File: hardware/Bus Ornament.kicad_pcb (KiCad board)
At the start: 4 copper layers, 110 x 57.8 mm, 35 parts, among them J1 Conn_02x03_Odd_Even, SW1 SW_SPST, SW2 SW_Push, U1 ATtiny85-20PU, U2 TPS62203DBV

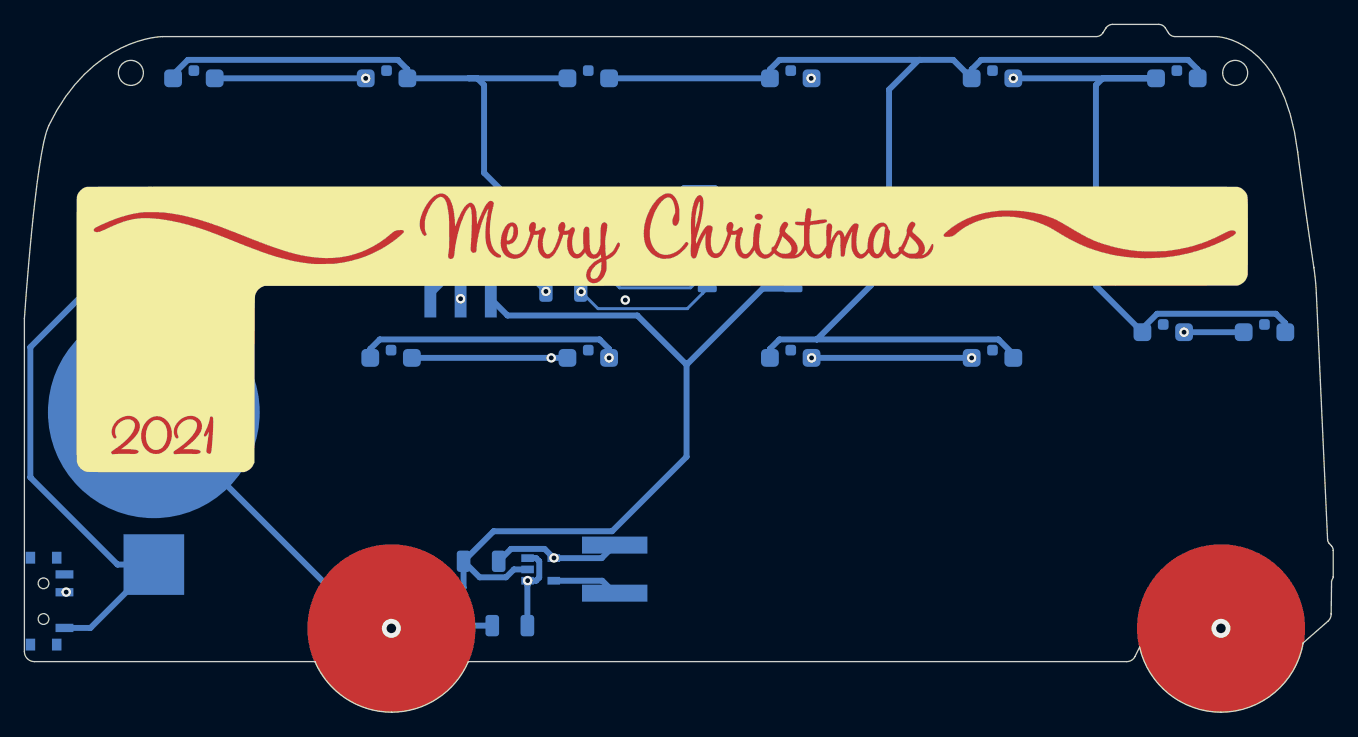
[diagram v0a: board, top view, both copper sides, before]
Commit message: Crated front fill, ordered new boards
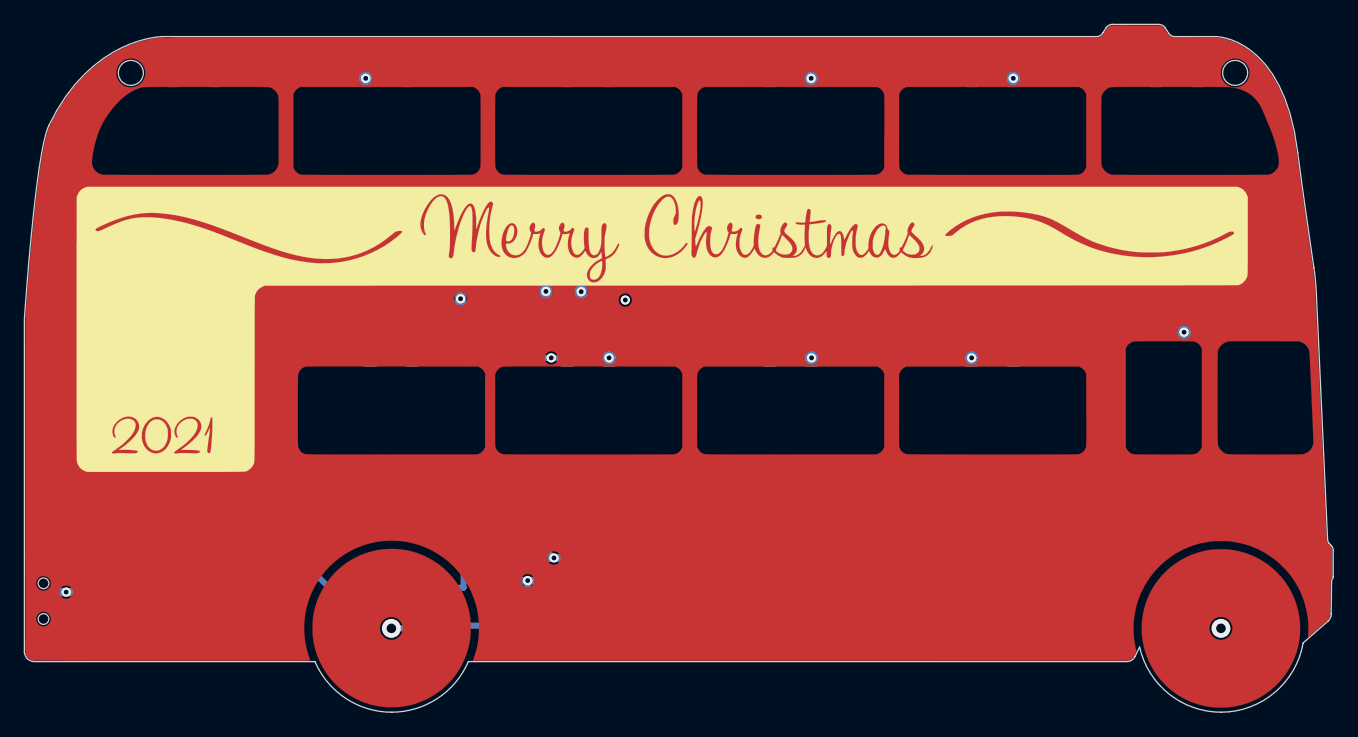
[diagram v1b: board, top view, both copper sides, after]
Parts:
- removed the G*** at (158.6, 132.6)
- removed the G*** at (88.9, 132.6)
- added G***: LOGO, artwork:front_copper_art, F.Cu at (113.1, 110.8)
